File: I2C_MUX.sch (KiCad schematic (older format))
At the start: 24 parts, among them U5 TCA9548ARGER

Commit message: bugs fixed
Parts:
- R45, R46, R47, R48, R49, R50, R51, R52, R53, R54, R55, R56, R57, R75, R83, R91: footprint RESC1005X40N -> Resistors SMD:RESC1005X40N; symbol Resistors_SMD:R0402_2K2_1%_0.0625W_100PPM -> Resistors_SMD:R0402_22K_1%_0.0625W_100PPM; Manufacturer Part Number R0402_2K2_1%_0.0625W_100PPM -> R0402_22K_1%_0.0625W_100PPM; Manufacturer1 Part Number 232270672202L -> 232270672203L; Part Number R0402_2K2_1%_0.0625W_100PPM -> R0402_22K_1%_0.0625W_100PPM; Val 2k2 -> 22k; ~ 2k2 -> 22k

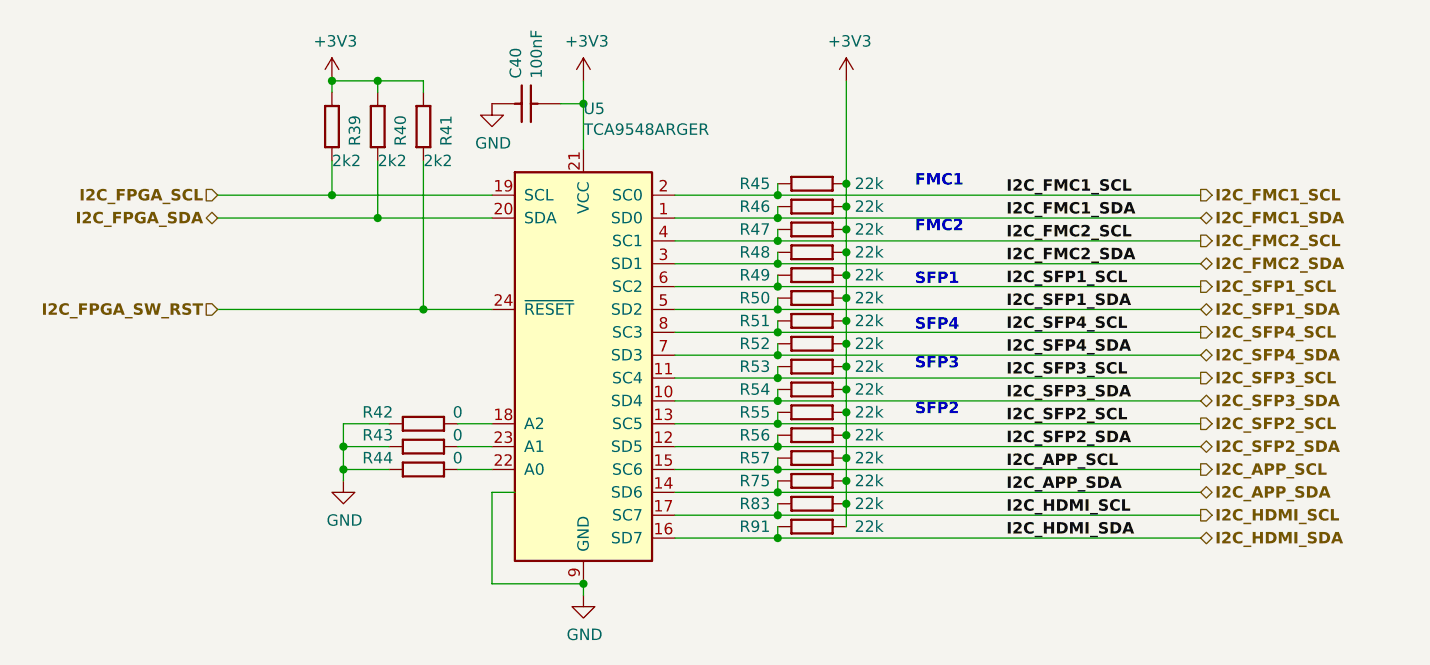
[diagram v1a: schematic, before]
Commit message: HDMI footprint changed, silk layer edited, bugs fixed
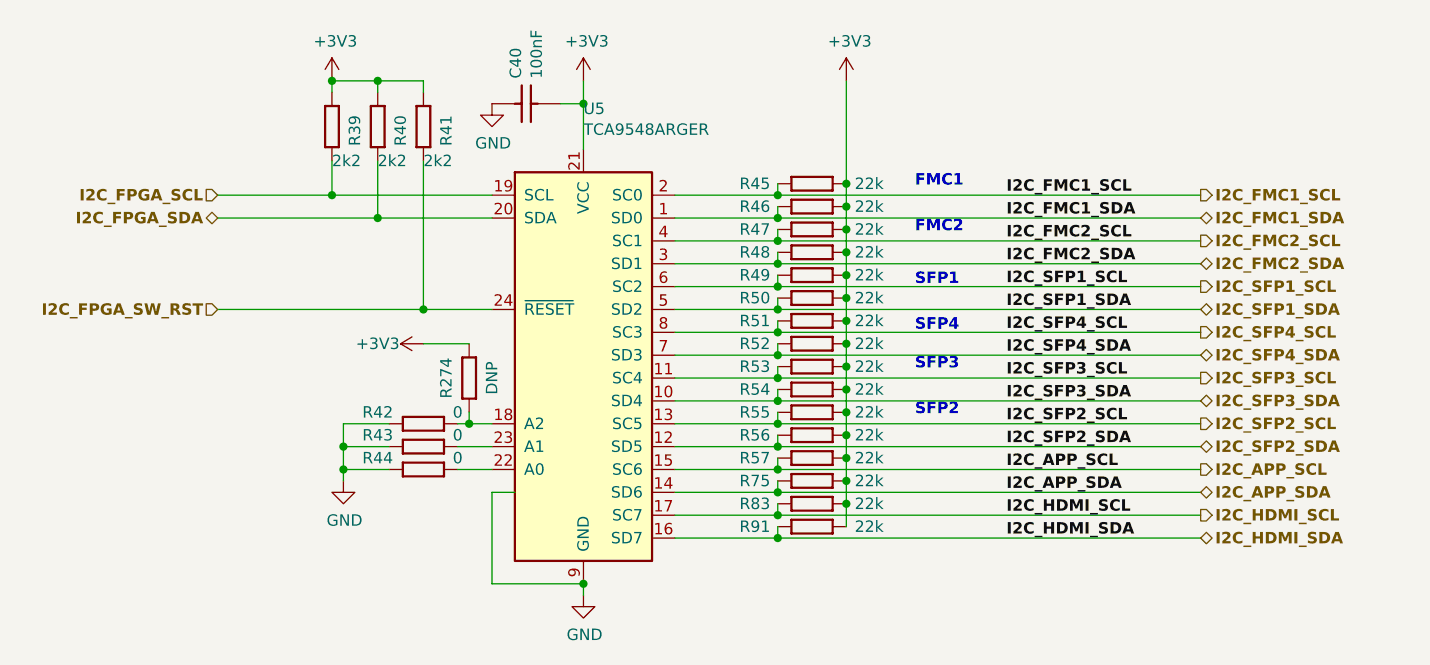
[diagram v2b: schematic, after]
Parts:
- added R274: R0402_0R_JUMPER, RESC1005X40N, symbol Resistors_SMD:R0402_0R_JUMPER
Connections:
- net +3V3: now also R274.1
- net at R42.1, U5.18 (A2): now also R274.2
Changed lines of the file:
@@
 	3550 2300 4250 2300
 Wire Wire Line
-	4600 3200 4750 3200
+	4600 3200 4650 3200
 Wire Wire Line
 	4600 3300 4750 3300
@@
 Data
 89 50 4E 47 0D 0A 1A 0A 00 00 00 0D 49 48 44 52 00 00 02 9C 00 00 01 94 08 06 00 00 00 98 F0 F2
-55 00 00 00 04 73 42 49 54 08 08 08 08 7C 08 64 88 00 00 00 09 70 48 59 73 00 00 0B 12 00 00 0B
-12 01 D2 DD 7E FC 00 00 20 00 49 44 41 54 78 9C EC BD BD 8E 3A 5D B6 E6 F9 AC D6 AB D2 A8 46 47
+55 00 00 00 04 73 42 49 54 08 08 08 08 7C 08 64 88 00 00 00 09 70 48 59 73 00 00 0A F0 00 00 0A
+F0 01 42 AC 34 98 00 00 20 00 49 44 41 54 78 9C EC BD BD 8E 3A 5D B6 E6 F9 AC D6 AB D2 A8 46 47
 23 5E E7 B4 54 46 49 A4 55 CE 94 74 48 BF 1D 52 EA 73 01 A4 7D D4 06 69 8F 45 5E 02 5C 02 38 E3
 27 17 50 06 18 7D 01 89 D3 7E 86 A6 BC 69 E7 4F 8D D4 66 49 6B 8C B5 36 6C 36 11 41 04 44 F0 15
@@
 EndData
 $EndBitmap
+$Comp
+L Resistors_SMD:R0402_0R_JUMPER R?
+U 1 1 5D00A0A2
+P 4650 2850
+AR Path="/5C16BF8E/5DB9B7E6/5D00A0A2" Ref="R?"  Part="1"
+AR Path="/5BCEDA3D/5D00A0A2" Ref="R274"  Part="1"
+F 0 "R274" H 4800 2750 50  0000 C CNN
+F 1 "R0402_0R_JUMPER" H 4650 2640 60  0001 L CNN
+F 2 "RESC1005X40N" H 4650 1830 60  0001 L CNN
+F 3 "\\\\cern.ch\\dfs\\Applications\\Altium\\Datasheets\\R0402_Phycomp_RC0402.pdf" H 4650 2460 60  0001 L CNN
+F 4 "DNP" H 4800 2950 50  0000 C CNN "~"
+F 5 "R0402_0R_JUMPER" H 4650 2370 60  0001 L CNN "Part Number"
+F 6 "Resistor" H 4650 2280 60  0001 L CNN "Library Ref"
+F 7 "SchLib\\Resistors.SchLib" H 4650 2190 60  0001 L CNN "Library Path"
+F 8 "=Value" H 4650 2100 60  0001 L CNN "Comment"
+F 9 "Standard" H 4650 2010 60  0001 L CNN "Component Kind"
+F 10 "Standard" H 4650 1920 60  0001 L CNN "Component Type"
+F 11 "~~" H 4650 1740 60  0001 L CNN "PackageDescription"
+F 12 "2" H 4650 1650 60  0001 L CNN "Pin Count"
+F 13 "PcbLib\\Resistors SMD.PcbLib" H 4650 1560 60  0001 L CNN "Footprint Path"
+F 14 "RESC1005X40N" H 4650 1470 60  0001 L CNN "Footprint Ref"
+F 15 "0" H 4650 1380 60  0001 L CNN "Val"
+F 16 "Not Recommended" H 4650 1290 60  0001 L CNN "Status"
+F 17 "~~" H 4650 1200 60  0001 L CNN "Power"
+F 18 "~~" H 4650 1110 60  0001 L CNN "TC"
+F 19 "~~" H 4650 1020 60  0001 L CNN "Voltage"
+F 20 "~~" H 4650 930 60  0001 L CNN "Tolerance"
+F 21 "1A (0.05R Max DC Resistance) Zero Ohm Jumper" H 4650 840 60  0001 L CNN "Part Description"
+F 22 "GENERIC" H 4650 750 60  0001 L CNN "Manufacturer"
+F 23 "R0402_0R_JUMPER" H 4650 660 60  0001 L CNN "Manufacturer Part Number"
+F 24 "0402" H 4650 570 60  0001 L CNN "Case"
+F 25 "No" H 4650 480 60  0001 L CNN "PressFit"
+F 26 "Yes" H 4650 390 60  0001 L CNN "Mounted"
+F 27 "~~" H 4650 300 60  0001 L CNN "Sense Comment"
+F 28 "No" H 4650 210 60  0001 L CNN "Sense"
+F 29 "~~" H 4650 120 60  0001 L CNN "Status Comment"
+F 30 "No" H 4650 30  60  0001 L CNN "Socket"
+F 31 "Yes" H 4650 -60 60  0001 L CNN "SMD"
+F 32 "~~" H 4650 -150 60  0001 L CNN "ComponentHeight"
+F 33 "YAGEO PHYCOMP" H 4650 -240 60  0001 L CNN "Manufacturer1 Example"
+F 34 "232270591001L" H 4650 -330 60  0001 L CNN "Manufacturer1 Part Number"
+F 35 "0.4mm" H 4650 -420 60  0001 L CNN "Manufacturer1 ComponentHeight"
+F 36 "\\\\cern.ch\\dfs\\Applications\\Altium\\Datasheets\\R0402_Phycomp_RC0402.pdf" H 4650 -510 60  0001 L CNN "HelpURL"
+F 37 "CERN DEM JLC" H 4650 -600 60  0001 L CNN "Author"
+F 38 "12/03/07 00:00:00" H 4650 -690 60  0001 L CNN "CreateDate"
+F 39 "10/17/12 00:00:00" H 4650 -780 60  0001 L CNN "LatestRevisionDate"
+F 40 "Resistors SMD" H 4650 -870 60  0001 L CNN "Library Name"
+F 41 "This work is licensed under the Creative Commons CC-BY-SA 4.0 License. To the extent that circuit schematics that use Licensed Material can be considered to be ‘Adapted Material’, then the copyright holder waives article 3.b of the license with respect to these schematics." H 4650 -960 60  0001 L CNN "License"
+	1    4650 2850
+	0    1    1    0
+$EndComp
+$Comp
+L power:+3V3 #PWR?
+U 1 1 5D00ED85
+P 4450 2850
+AR Path="/5BD32060/5D00ED85" Ref="#PWR?"  Part="1"
+AR Path="/5BABAC65/5D00ED85" Ref="#PWR?"  Part="1"
+AR Path="/5CC24E97/5D00ED85" Ref="#PWR?"  Part="1"
+AR Path="/5CC393D3/5D00ED85" Ref="#PWR?"  Part="1"
+AR Path="/5CC6DBF7/5D00ED85" Ref="#PWR?"  Part="1"
+AR Path="/5CC8AFE1/5D00ED85" Ref="#PWR?"  Part="1"
+AR Path="/5BCEDA3D/5D00ED85" Ref="#PWR0648"  Part="1"
+F 0 "#PWR0648" H 4450 2700 50  0001 C CNN
+F 1 "+3V3" V 4450 3050 50  0000 C CNN
+F 2 "" H 4450 2850 50  0001 C CNN
+F 3 "" H 4450 2850 50  0001 C CNN
+	1    4450 2850
+	0    -1   -1   0
+$EndComp
+Wire Wire Line
+	4450 2850 4650 2850
+Wire Wire Line
+	4650 3150 4650 3200
+Connection ~ 4650 3200
+Wire Wire Line
+	4650 3200 4750 3200
 $EndSCHEMATC

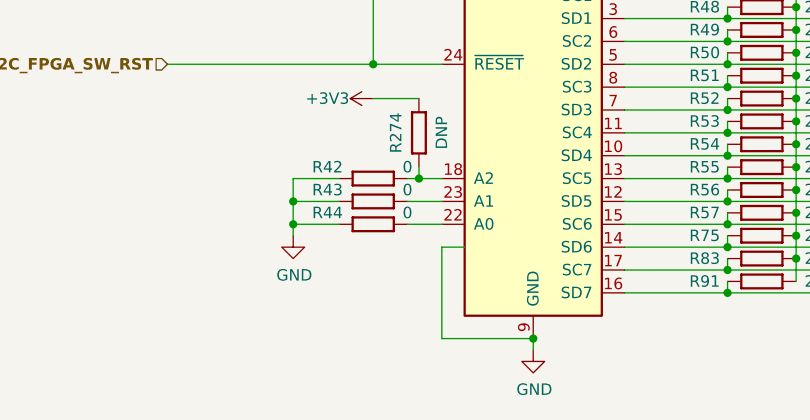
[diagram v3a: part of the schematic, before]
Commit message: new FMC JTAG chain
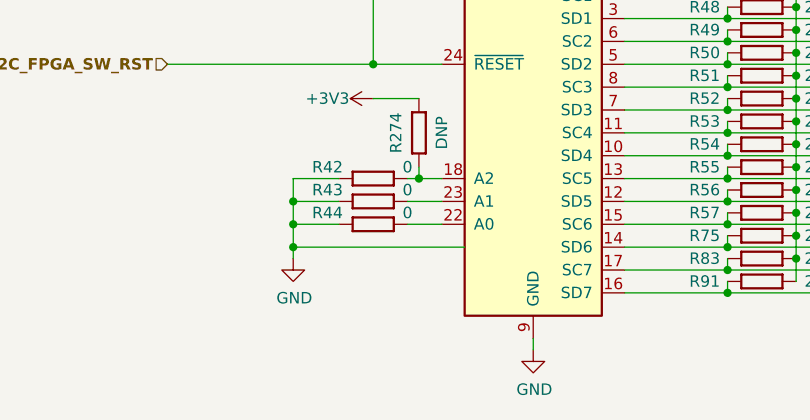
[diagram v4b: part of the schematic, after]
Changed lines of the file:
@@
 L power:GND #PWR?
 U 1 1 5C2ECB8E
-P 4100 3450
+P 4100 3550
 AR Path="/5BD32060/5C2ECB8E" Ref="#PWR?"  Part="1"
 AR Path="/5BABAC65/5C2ECB8E" Ref="#PWR?"  Part="1"
@@
 AR Path="/5CC8AFE1/5C2ECB8E" Ref="#PWR?"  Part="1"
 AR Path="/5BCEDA3D/5C2ECB8E" Ref="#PWR063"  Part="1"
-F 0 "#PWR063" H 4100 3200 50  0001 C CNN
-F 1 "GND" H 4105 3277 50  0000 C CNN
-F 2 "" H 4100 3450 50  0001 C CNN
-F 3 "" H 4100 3450 50  0001 C CNN
-	1    4100 3450
+F 0 "#PWR063" H 4100 3300 50  0001 C CNN
+F 1 "GND" H 4105 3377 50  0000 C CNN
+F 2 "" H 4100 3550 50  0001 C CNN
+F 3 "" H 4100 3550 50  0001 C CNN
+	1    4100 3550
 	1    0    0    -1
 $EndComp
@@
 	4300 3400 4100 3400
 Connection ~ 4100 3400
-Wire Wire Line
-	4100 3400 4100 3450
 Text HLabel 3550 2300 0    50   BiDi ~ 10
 I2C_FPGA_SDA
@@
 Connection ~ 6000 3200
 Connection ~ 6000 3300
-Wire Wire Line
-	4850 3500 4750 3500
-Wire Wire Line
-	4750 3500 4750 3900
-Wire Wire Line
-	4750 3900 5150 3900
-Connection ~ 5150 3900
 $Bitmap
 Pos 3850 5900
@@
 Wire Wire Line
 	4650 3200 4750 3200
+Wire Wire Line
+	4100 3500 4100 3550
+Wire Wire Line
+	4100 3500 4850 3500
+Wire Wire Line
+	4100 3400 4100 3500
+Connection ~ 4100 3500
 $EndSCHEMATC

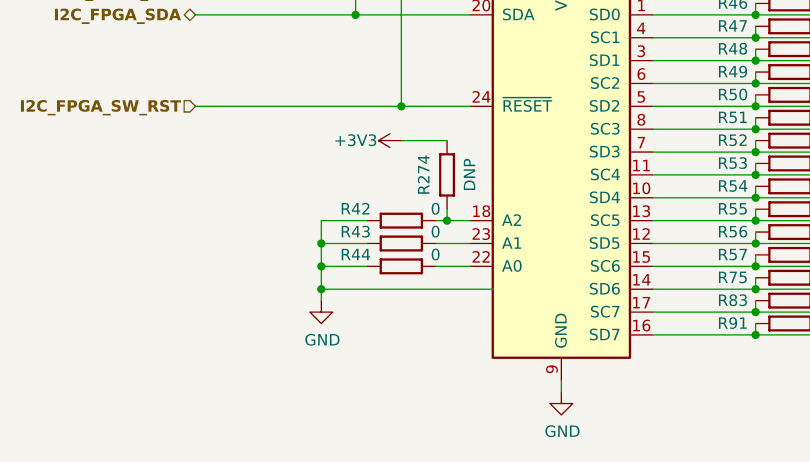
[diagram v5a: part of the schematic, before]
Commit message: ERC bugs fixed
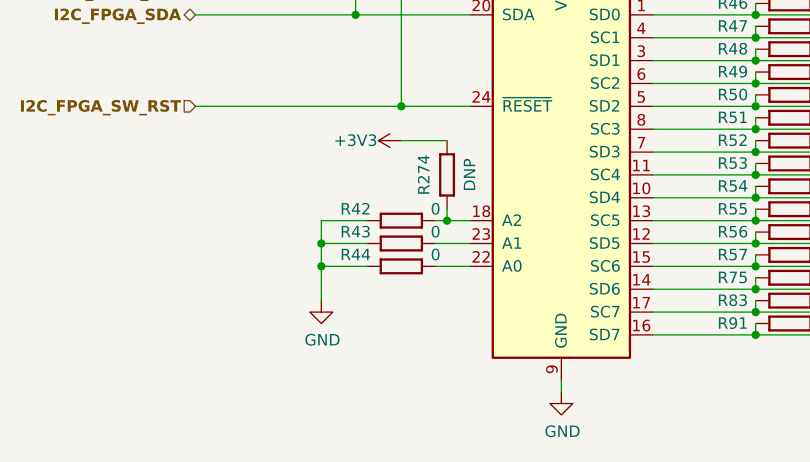
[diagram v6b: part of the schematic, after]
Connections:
- net GND: no longer U5.25 (1EP)
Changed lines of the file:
@@
 	4650 3200 4750 3200
 Wire Wire Line
-	4100 3500 4100 3550
-Wire Wire Line
-	4100 3500 4850 3500
-Wire Wire Line
-	4100 3400 4100 3500
-Connection ~ 4100 3500
+	4100 3400 4100 3550
 $EndSCHEMATC
